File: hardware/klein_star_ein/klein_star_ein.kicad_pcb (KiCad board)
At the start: 6 copper layers, 171 parts, among them J1 USB_A, J2 DB15_Female_HighDensity_Mount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, U1 ECP5UM25, U2 MT41K512M16, U3 MT41K512M16, U4 FT2232HQ, U5 W25Q128JVS, U6 USB3300-EZK, U7 USB3300-EZK

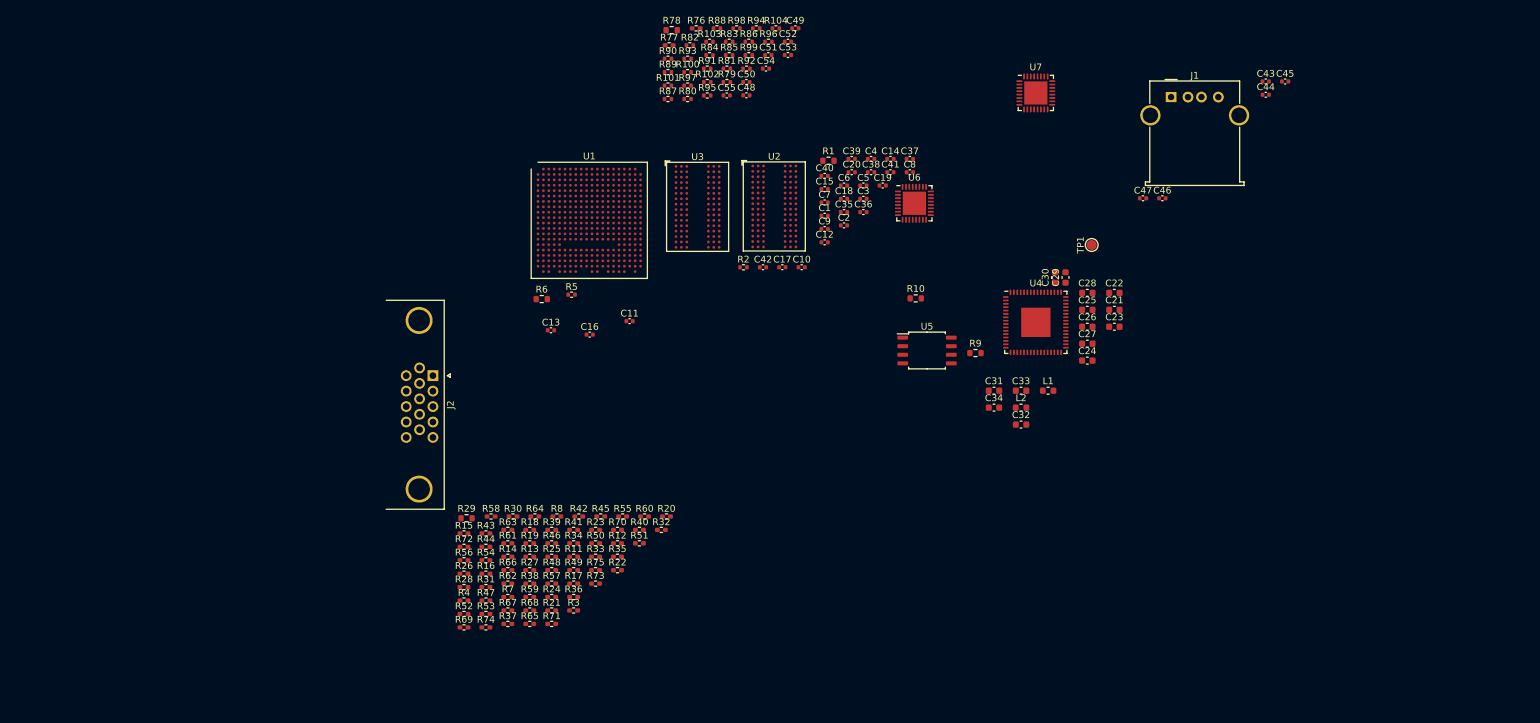
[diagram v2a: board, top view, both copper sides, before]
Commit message: VGA phy schematic and layout
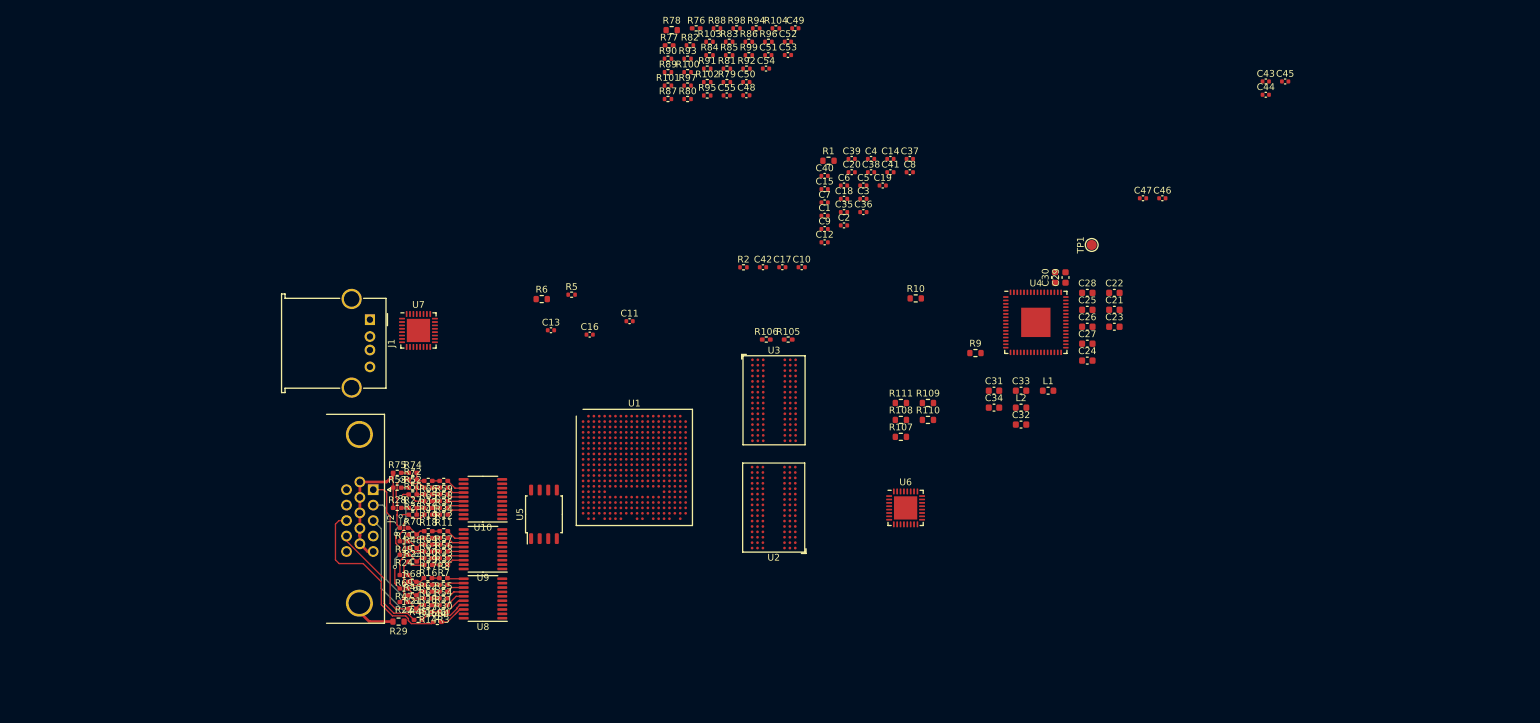
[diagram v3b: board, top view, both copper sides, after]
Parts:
- removed R13, R20, R26, R36, R43, R51, R60, R67, R73: R, Resistor_SMD:R_0402_1005Metric_Pad0.72x0.64mm_HandSolder
- added R105: 0R, Resistor_SMD:R_0402_1005Metric_Pad0.72x0.64mm_HandSolder, F.Cu at (167.2, 106.4)
- added R106: 0R, Resistor_SMD:R_0402_1005Metric_Pad0.72x0.64mm_HandSolder, F.Cu at (163.9, 106.4)
- added R107: 10k, Resistor_SMD:R_0603_1608Metric, F.Cu at (183.8, 120.8)
- added R108: 0R, Resistor_SMD:R_0603_1608Metric, F.Cu at (183.8, 118.3)
- added R109: 0R, Resistor_SMD:R_0603_1608Metric, F.Cu at (187.9, 115.8)
- added R110: 0R, Resistor_SMD:R_0603_1608Metric, F.Cu at (187.9, 118.3)
- added R111: 0R, Resistor_SMD:R_0603_1608Metric, F.Cu at (183.8, 115.8)
- added U10: SN74ALVC245PWR, Package_SO:TSSOP-20_4.4x6.5mm_P0.65mm, F.Cu at (121.9, 130.1)
- added U8: SN74ALVC245PWR, Package_SO:TSSOP-20_4.4x6.5mm_P0.65mm, F.Cu at (121.9, 144.8)
- added U9: SN74ALVC245PWR, Package_SO:TSSOP-20_4.4x6.5mm_P0.65mm, F.Cu at (121.9, 137.5)
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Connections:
- net Net-(U6-Pad14) renamed /USB_SLAVE_CLKOUT
- net Net-(U6-Pad28) renamed /USB_SLAVE_CLK
- net Net-(U6-Pad9) renamed /USB_SLAVE_RESET
- J1 pad 1: Net-(J1-Pad1) -> unconnected-(J1-Pad1)
- J2 pad 11: no_connect_462 -> unconnected-(J2-Pad11)
- J2 pad 12: no_connect_463 -> unconnected-(J2-Pad12)
- J2 pad 15: no_connect_464 -> unconnected-(J2-Pad15)
- J2 pad 4: no_connect_465 -> unconnected-(J2-Pad4)
- R27 pad 2: Net-(R20-Pad2) -> Net-(R19-Pad2)
- R52 pad 2: Net-(R43-Pad2) -> Net-(R42-Pad2)
- R74 pad 2: Net-(R67-Pad2) -> Net-(R66-Pad2)
- U1 pad A12: Net-(U1-PadA12) -> unconnected-(U1-PadA12)
- U1 pad A13: Net-(U1-PadA13) -> unconnected-(U1-PadA13)
- U1 pad A14: Net-(U1-PadA14) -> unconnected-(U1-PadA14)
- U1 pad A15: no_connect_466 -> unconnected-(U1-PadA15)
- U1 pad A16: Net-(U1-PadA16) -> unconnected-(U1-PadA16)
- U1 pad A17: Net-(U1-PadA17) -> unconnected-(U1-PadA17)
- U1 pad A18: Net-(U1-PadA18) -> unconnected-(U1-PadA18)
- U1 pad A19: Net-(U1-PadA19) -> unconnected-(U1-PadA19)
- U1 pad A2: Net-(U1-PadA2) -> unconnected-(U1-PadA2)
- U1 pad A3: Net-(U1-PadA3) -> unconnected-(U1-PadA3)
- U1 pad A4: Net-(U1-PadA4) -> unconnected-(U1-PadA4)
- U1 pad A5: Net-(U1-PadA5) -> unconnected-(U1-PadA5)
- U1 pad B1: Net-(U1-PadB1) -> unconnected-(U1-PadB1)
- U1 pad B12: Net-(U1-PadB12) -> unconnected-(U1-PadB12)
- U1 pad B13: Net-(U1-PadB13) -> unconnected-(U1-PadB13)
- U1 pad B15: Net-(U1-PadB15) -> unconnected-(U1-PadB15)
- U1 pad B16: Net-(U1-PadB16) -> unconnected-(U1-PadB16)
- U1 pad B17: Net-(U1-PadB17) -> unconnected-(U1-PadB17)
- U1 pad B18: Net-(U1-PadB18) -> unconnected-(U1-PadB18)
- U1 pad B19: Net-(U1-PadB19) -> unconnected-(U1-PadB19)
- U1 pad B2: Net-(U1-PadB2) -> unconnected-(U1-PadB2)
- U1 pad B20: Net-(U1-PadB20) -> unconnected-(U1-PadB20)
- U1 pad B3: Net-(U1-PadB3) -> unconnected-(U1-PadB3)
- U1 pad B4: Net-(U1-PadB4) -> unconnected-(U1-PadB4)
- U1 pad B5: Net-(U1-PadB5) -> unconnected-(U1-PadB5)
- U1 pad C1: Net-(U1-PadC1) -> unconnected-(U1-PadC1)
- U1 pad C12: Net-(U1-PadC12) -> unconnected-(U1-PadC12)
- U1 pad C13: Net-(U1-PadC13) -> unconnected-(U1-PadC13)
- U1 pad C14: Net-(U1-PadC14) -> unconnected-(U1-PadC14)
- U1 pad C15: Net-(U1-PadC15) -> unconnected-(U1-PadC15)
- U1 pad C16: Net-(U1-PadC16) -> unconnected-(U1-PadC16)
- U1 pad C17: Net-(U1-PadC17) -> unconnected-(U1-PadC17)
- U1 pad C18: Net-(U1-PadC18) -> unconnected-(U1-PadC18)
- U1 pad C2: Net-(U1-PadC2) -> unconnected-(U1-PadC2)
- U1 pad C20: Net-(U1-PadC20) -> unconnected-(U1-PadC20)
- U1 pad C3: Net-(U1-PadC3) -> unconnected-(U1-PadC3)
- U1 pad C4: Net-(U1-PadC4) -> unconnected-(U1-PadC4)
- U1 pad C5: Net-(U1-PadC5) -> unconnected-(U1-PadC5)
- U1 pad C9: no_connect_467 -> unconnected-(U1-PadC9)
- U1 pad D1: Net-(U1-PadD1) -> unconnected-(U1-PadD1)
- U1 pad D10: no_connect_468 -> unconnected-(U1-PadD10)
- U1 pad D11: Net-(U1-PadD11) -> unconnected-(U1-PadD11)
- U1 pad D12: Net-(U1-PadD12) -> unconnected-(U1-PadD12)
- U1 pad D13: Net-(U1-PadD13) -> unconnected-(U1-PadD13)
- U1 pad D14: Net-(U1-PadD14) -> unconnected-(U1-PadD14)
- U1 pad D15: Net-(U1-PadD15) -> unconnected-(U1-PadD15)
- U1 pad D16: Net-(U1-PadD16) -> unconnected-(U1-PadD16)
- U1 pad D17: Net-(U1-PadD17) -> unconnected-(U1-PadD17)
- U1 pad D18: Net-(U1-PadD18) -> unconnected-(U1-PadD18)
- U1 pad D19: Net-(U1-PadD19) -> unconnected-(U1-PadD19)
- U1 pad D2: Net-(U1-PadD2) -> unconnected-(U1-PadD2)
- U1 pad D20: Net-(U1-PadD20) -> unconnected-(U1-PadD20)
- U1 pad D3: Net-(U1-PadD3) -> unconnected-(U1-PadD3)
- U1 pad D5: Net-(U1-PadD5) -> unconnected-(U1-PadD5)
- U1 pad E1: Net-(U1-PadE1) -> unconnected-(U1-PadE1)
- U1 pad E10: no_connect_469 -> unconnected-(U1-PadE10)
- U1 pad E11: Net-(U1-PadE11) -> unconnected-(U1-PadE11)
- U1 pad E12: Net-(U1-PadE12) -> unconnected-(U1-PadE12)
- U1 pad E13: Net-(U1-PadE13) -> unconnected-(U1-PadE13)
- U1 pad E14: Net-(U1-PadE14) -> unconnected-(U1-PadE14)
- U1 pad E15: Net-(U1-PadE15) -> unconnected-(U1-PadE15)
- U1 pad E16: Net-(U1-PadE16) -> unconnected-(U1-PadE16)
- U1 pad E17: Net-(U1-PadE17) -> unconnected-(U1-PadE17)
- U1 pad E18: Net-(U1-PadE18) -> unconnected-(U1-PadE18)
- U1 pad E19: Net-(U1-PadE19) -> unconnected-(U1-PadE19)
- U1 pad E2: Net-(U1-PadE2) -> unconnected-(U1-PadE2)
- U1 pad E20: Net-(U1-PadE20) -> unconnected-(U1-PadE20)
- U1 pad E3: Net-(U1-PadE3) -> unconnected-(U1-PadE3)
- U1 pad E4: Net-(U1-PadE4) -> unconnected-(U1-PadE4)
- U1 pad E5: Net-(U1-PadE5) -> unconnected-(U1-PadE5)
- U1 pad F1: Net-(U1-PadF1) -> unconnected-(U1-PadF1)
- U1 pad F10: Net-(U1-PadF10) -> unconnected-(U1-PadF10)
- U1 pad F11: Net-(U1-PadF11) -> unconnected-(U1-PadF11)
- U1 pad F12: Net-(U1-PadF12) -> unconnected-(U1-PadF12)
- U1 pad F15: Net-(U1-PadF15) -> unconnected-(U1-PadF15)
- U1 pad F16: Net-(U1-PadF16) -> unconnected-(U1-PadF16)
- U1 pad F17: Net-(U1-PadF17) -> unconnected-(U1-PadF17)
- U1 pad F18: Net-(U1-PadF18) -> unconnected-(U1-PadF18)
- U1 pad F19: Net-(U1-PadF19) -> unconnected-(U1-PadF19)
- U1 pad F2: Net-(U1-PadF2) -> unconnected-(U1-PadF2)
- U1 pad F20: Net-(U1-PadF20) -> unconnected-(U1-PadF20)
- U1 pad F3: Net-(U1-PadF3) -> unconnected-(U1-PadF3)
- U1 pad F4: Net-(U1-PadF4) -> unconnected-(U1-PadF4)
- U1 pad F5: Net-(U1-PadF5) -> unconnected-(U1-PadF5)
- U1 pad F6: Net-(U1-PadF6) -> unconnected-(U1-PadF6)
- U1 pad F9: Net-(U1-PadF9) -> unconnected-(U1-PadF9)
- U1 pad G1: Net-(U1-PadG1) -> unconnected-(U1-PadG1)
- U1 pad G16: Net-(U1-PadG16) -> unconnected-(U1-PadG16)
- U1 pad G18: Net-(U1-PadG18) -> unconnected-(U1-PadG18)
- U1 pad G19: Net-(U1-PadG19) -> unconnected-(U1-PadG19)
- U1 pad G2: Net-(U1-PadG2) -> unconnected-(U1-PadG2)
- U1 pad G20: Net-(U1-PadG20) -> unconnected-(U1-PadG20)
- U1 pad G3: Net-(U1-PadG3) -> unconnected-(U1-PadG3)
- U1 pad G5: Net-(U1-PadG5) -> unconnected-(U1-PadG5)
- U1 pad H1: Net-(U1-PadH1) -> unconnected-(U1-PadH1)
- U1 pad H10: Net-(U1-PadH10) -> unconnected-(U1-PadH10)
- U1 pad H11: Net-(U1-PadH11) -> unconnected-(U1-PadH11)
- U1 pad H12: Net-(U1-PadH12) -> unconnected-(U1-PadH12)
- U1 pad H13: Net-(U1-PadH13) -> unconnected-(U1-PadH13)
- U1 pad H14: Net-(U1-PadH14) -> unconnected-(U1-PadH14)
- U1 pad H15: Net-(U1-PadH15) -> unconnected-(U1-PadH15)
- U1 pad H16: Net-(U1-PadH16) -> unconnected-(U1-PadH16)
- U1 pad H17: Net-(U1-PadH17) -> unconnected-(U1-PadH17)
- U1 pad H18: Net-(U1-PadH18) -> unconnected-(U1-PadH18)
- U1 pad H2: Net-(U1-PadH2) -> unconnected-(U1-PadH2)
- U1 pad H20: Net-(U1-PadH20) -> unconnected-(U1-PadH20)
- U1 pad H3: Net-(U1-PadH3) -> unconnected-(U1-PadH3)
- U1 pad H4: Net-(U1-PadH4) -> unconnected-(U1-PadH4)
- U1 pad H5: Net-(U1-PadH5) -> unconnected-(U1-PadH5)
- U1 pad H6: Net-(U1-PadH6) -> unconnected-(U1-PadH6)
- U1 pad H7: Net-(U1-PadH7) -> unconnected-(U1-PadH7)
- U1 pad H8: Net-(U1-PadH8) -> unconnected-(U1-PadH8)
- U1 pad H9: Net-(U1-PadH9) -> unconnected-(U1-PadH9)
- U1 pad J1: Net-(U1-PadJ1) -> unconnected-(U1-PadJ1)
- U1 pad J13: Net-(U1-PadJ13) -> unconnected-(U1-PadJ13)
- U1 pad J15: Net-(U1-PadJ15) -> unconnected-(U1-PadJ15)
- U1 pad J16: Net-(U1-PadJ16) -> unconnected-(U1-PadJ16)
- U1 pad J17: Net-(U1-PadJ17) -> unconnected-(U1-PadJ17)
- U1 pad J18: Net-(U1-PadJ18) -> unconnected-(U1-PadJ18)
- U1 pad J19: Net-(U1-PadJ19) -> unconnected-(U1-PadJ19)
- U1 pad J20: Net-(U1-PadJ20) -> unconnected-(U1-PadJ20)
- U1 pad J3: Net-(U1-PadJ3) -> unconnected-(U1-PadJ3)
- U1 pad J4: Net-(U1-PadJ4) -> unconnected-(U1-PadJ4)
- U1 pad J5: Net-(U1-PadJ5) -> unconnected-(U1-PadJ5)
- U1 pad J6: Net-(U1-PadJ6) -> unconnected-(U1-PadJ6)
- U1 pad J8: Net-(U1-PadJ8) -> unconnected-(U1-PadJ8)
- U1 pad K1: Net-(U1-PadK1) -> unconnected-(U1-PadK1)
- U1 pad K13: Net-(U1-PadK13) -> unconnected-(U1-PadK13)
- U1 pad K16: no_connect_470 -> unconnected-(U1-PadK16)
- U1 pad K17: no_connect_471 -> unconnected-(U1-PadK17)
- U1 pad K18: Net-(U1-PadK18) -> unconnected-(U1-PadK18)
- U1 pad K19: Net-(U1-PadK19) -> unconnected-(U1-PadK19)
- U1 pad K2: Net-(U1-PadK2) -> unconnected-(U1-PadK2)
- U1 pad K20: Net-(U1-PadK20) -> unconnected-(U1-PadK20)
- U1 pad K3: Net-(U1-PadK3) -> unconnected-(U1-PadK3)
- U1 pad K4: Net-(U1-PadK4) -> unconnected-(U1-PadK4)
- U1 pad K5: Net-(U1-PadK5) -> unconnected-(U1-PadK5)
- U1 pad K8: Net-(U1-PadK8) -> unconnected-(U1-PadK8)
- U1 pad L1: Net-(U1-PadL1) -> unconnected-(U1-PadL1)
- U1 pad L13: Net-(U1-PadL13) -> unconnected-(U1-PadL13)
- U1 pad L14: Net-(U1-PadL14) -> unconnected-(U1-PadL14)
- U1 pad L15: Net-(U1-PadL15) -> unconnected-(U1-PadL15)
- U1 pad L16: Net-(U1-PadL16) -> unconnected-(U1-PadL16)
- U1 pad L17: Net-(U1-PadL17) -> unconnected-(U1-PadL17)
- U1 pad L18: Net-(U1-PadL18) -> unconnected-(U1-PadL18)
- U1 pad L19: Net-(U1-PadL19) -> unconnected-(U1-PadL19)
- U1 pad L2: Net-(U1-PadL2) -> unconnected-(U1-PadL2)
- U1 pad L20: Net-(U1-PadL20) -> unconnected-(U1-PadL20)
- U1 pad L3: Net-(U1-PadL3) -> unconnected-(U1-PadL3)
- U1 pad L4: Net-(U1-PadL4) -> unconnected-(U1-PadL4)
- U1 pad L5: Net-(U1-PadL5) -> unconnected-(U1-PadL5)
- U1 pad L6: Net-(U1-PadL6) -> unconnected-(U1-PadL6)
- U1 pad L7: Net-(U1-PadL7) -> unconnected-(U1-PadL7)
- U1 pad L8: Net-(U1-PadL8) -> unconnected-(U1-PadL8)
- U1 pad M1: Net-(U1-PadM1) -> unconnected-(U1-PadM1)
- U1 pad M13: Net-(U1-PadM13) -> unconnected-(U1-PadM13)
- U1 pad M15: Net-(U1-PadM15) -> unconnected-(U1-PadM15)
- U1 pad M17: Net-(U1-PadM17) -> unconnected-(U1-PadM17)
- U1 pad M18: Net-(U1-PadM18) -> unconnected-(U1-PadM18)
- U1 pad M19: Net-(U1-PadM19) -> unconnected-(U1-PadM19)
- U1 pad M20: Net-(U1-PadM20) -> unconnected-(U1-PadM20)
- U1 pad M3: Net-(U1-PadM3) -> unconnected-(U1-PadM3)
- U1 pad M4: Net-(U1-PadM4) -> unconnected-(U1-PadM4)
- U1 pad M5: no_connect_472 -> unconnected-(U1-PadM5)
- U1 pad M6: Net-(U1-PadM6) -> unconnected-(U1-PadM6)
- U1 pad M8: Net-(U1-PadM8) -> unconnected-(U1-PadM8)
- U1 pad N1: Net-(U1-PadN1) -> unconnected-(U1-PadN1)
- U1 pad N10: Net-(U1-PadN10) -> unconnected-(U1-PadN10)
- U1 pad N11: Net-(U1-PadN11) -> unconnected-(U1-PadN11)
- U1 pad N12: Net-(U1-PadN12) -> unconnected-(U1-PadN12)
- U1 pad N13: Net-(U1-PadN13) -> unconnected-(U1-PadN13)
- U1 pad N16: Net-(U1-PadN16) -> unconnected-(U1-PadN16)
- U1 pad N17: Net-(U1-PadN17) -> unconnected-(U1-PadN17)
- U1 pad N18: Net-(U1-PadN18) -> unconnected-(U1-PadN18)
- U1 pad N19: Net-(U1-PadN19) -> unconnected-(U1-PadN19)
- U1 pad N2: Net-(U1-PadN2) -> unconnected-(U1-PadN2)
- U1 pad N20: Net-(U1-PadN20) -> unconnected-(U1-PadN20)
- U1 pad N3: Net-(U1-PadN3) -> unconnected-(U1-PadN3)
- U1 pad N4: Net-(U1-PadN4) -> unconnected-(U1-PadN4)
- U1 pad N5: Net-(U1-PadN5) -> unconnected-(U1-PadN5)
- U1 pad N8: Net-(U1-PadN8) -> unconnected-(U1-PadN8)
- U1 pad N9: Net-(U1-PadN9) -> unconnected-(U1-PadN9)
- U1 pad P1: Net-(U1-PadP1) -> unconnected-(U1-PadP1)
- U1 pad P15: Net-(U1-PadP15) -> unconnected-(U1-PadP15)
- U1 pad P16: Net-(U1-PadP16) -> unconnected-(U1-PadP16)
- U1 pad P17: Net-(U1-PadP17) -> unconnected-(U1-PadP17)
- U1 pad P18: Net-(U1-PadP18) -> unconnected-(U1-PadP18)
- U1 pad P19: Net-(U1-PadP19) -> unconnected-(U1-PadP19)
- U1 pad P2: Net-(U1-PadP2) -> unconnected-(U1-PadP2)
- U1 pad P20: Net-(U1-PadP20) -> unconnected-(U1-PadP20)
- U1 pad P3: Net-(U1-PadP3) -> unconnected-(U1-PadP3)
- U1 pad P4: Net-(U1-PadP4) -> unconnected-(U1-PadP4)
- U1 pad P5: Net-(U1-PadP5) -> unconnected-(U1-PadP5)
- U1 pad P6: Net-(U1-PadP6) -> unconnected-(U1-PadP6)
- U1 pad R16: Net-(U1-PadR16) -> unconnected-(U1-PadR16)
- U1 pad R17: Net-(U1-PadR17) -> unconnected-(U1-PadR17)
- U1 pad R18: Net-(U1-PadR18) -> unconnected-(U1-PadR18)
- U1 pad R20: Net-(U1-PadR20) -> unconnected-(U1-PadR20)
- U1 pad R5: Net-(U1-PadR5) -> unconnected-(U1-PadR5)
- U1 pad T10: Net-(U1-PadT10) -> unconnected-(U1-PadT10)
- U1 pad T11: no_connect_473 -> unconnected-(U1-PadT11)
- U1 pad T12: no_connect_474 -> unconnected-(U1-PadT12)
- U1 pad T13: no_connect_475 -> unconnected-(U1-PadT13)
- U1 pad T14: no_connect_476 -> unconnected-(U1-PadT14)
- U1 pad T15: no_connect_477 -> unconnected-(U1-PadT15)
- U1 pad T16: no_connect_478 -> unconnected-(U1-PadT16)
- U1 pad T17: Net-(U1-PadT17) -> unconnected-(U1-PadT17)
- U1 pad T18: Net-(U1-PadT18) -> unconnected-(U1-PadT18)
- U1 pad T19: Net-(U1-PadT19) -> unconnected-(U1-PadT19)
- U1 pad T20: Net-(U1-PadT20) -> unconnected-(U1-PadT20)
- U1 pad T5: Net-(U1-PadT5) -> unconnected-(U1-PadT5)
- U1 pad T6: Net-(U1-PadT6) -> unconnected-(U1-PadT6)
- U1 pad T7: Net-(U1-PadT7) -> unconnected-(U1-PadT7)
- U1 pad T8: Net-(U1-PadT8) -> unconnected-(U1-PadT8)
- U1 pad T9: Net-(U1-PadT9) -> unconnected-(U1-PadT9)
- U1 pad U15: no_connect_479 -> unconnected-(U1-PadU15)
- U1 pad U16: Net-(U1-PadU16) -> unconnected-(U1-PadU16)
- U1 pad U17: Net-(U1-PadU17) -> unconnected-(U1-PadU17)
- U1 pad U18: Net-(U1-PadU18) -> unconnected-(U1-PadU18)
- U1 pad U19: Net-(U1-PadU19) -> unconnected-(U1-PadU19)
- U1 pad U20: Net-(U1-PadU20) -> unconnected-(U1-PadU20)
- U1 pad U5: Net-(U1-PadU5) -> unconnected-(U1-PadU5)
- U1 pad U6: Net-(U1-PadU6) -> unconnected-(U1-PadU6)
- U1 pad V10: Net-(U1-PadV10) -> unconnected-(U1-PadV10)
- U1 pad V11: Net-(U1-PadV11) -> unconnected-(U1-PadV11)
- U1 pad V17: no_connect_480 -> unconnected-(U1-PadV17)
- U1 pad V18: no_connect_481 -> unconnected-(U1-PadV18)
- U1 pad V4: Net-(U1-PadV4) -> unconnected-(U1-PadV4)
- U1 pad W10: Net-(U1-PadW10) -> unconnected-(U1-PadW10)
- U1 pad W11: Net-(U1-PadW11) -> unconnected-(U1-PadW11)
- U1 pad W13: no_connect_482 -> unconnected-(U1-PadW13)
- U1 pad W14: no_connect_483 -> unconnected-(U1-PadW14)
- U1 pad W17: no_connect_484 -> unconnected-(U1-PadW17)
- U1 pad W18: no_connect_485 -> unconnected-(U1-PadW18)
- U1 pad W20: no_connect_486 -> unconnected-(U1-PadW20)
- U1 pad W4: Net-(U1-PadW4) -> unconnected-(U1-PadW4)
- U1 pad W5: Net-(U1-PadW5) -> unconnected-(U1-PadW5)
- U1 pad W8: Net-(U1-PadW8) -> unconnected-(U1-PadW8)
- U1 pad W9: Net-(U1-PadW9) -> unconnected-(U1-PadW9)
- U1 pad Y11: Net-(U1-PadY11) -> unconnected-(U1-PadY11)
- U1 pad Y12: Net-(U1-PadY12) -> unconnected-(U1-PadY12)
- U1 pad Y14: no_connect_487 -> unconnected-(U1-PadY14)
- U1 pad Y15: no_connect_488 -> unconnected-(U1-PadY15)
- U1 pad Y16: no_connect_489 -> unconnected-(U1-PadY16)
- U1 pad Y17: no_connect_490 -> unconnected-(U1-PadY17)
- U1 pad Y19: no_connect_491 -> unconnected-(U1-PadY19)
- U1 pad Y5: Net-(U1-PadY5) -> unconnected-(U1-PadY5)
- U1 pad Y6: Net-(U1-PadY6) -> unconnected-(U1-PadY6)
- U1 pad Y7: Net-(U1-PadY7) -> unconnected-(U1-PadY7)
- U1 pad Y8: Net-(U1-PadY8) -> unconnected-(U1-PadY8)
- U2 pad J1: no_connect_492 -> unconnected-(U2-PadJ1)
- U2 pad J9: no_connect_493 -> unconnected-(U2-PadJ9)
- U2 pad L1: no_connect_494 -> unconnected-(U2-PadL1)
- U2 pad L9: no_connect_495 -> unconnected-(U2-PadL9)
- U3 pad J1: no_connect_496 -> unconnected-(U3-PadJ1)
- U3 pad J9: no_connect_497 -> unconnected-(U3-PadJ9)
- U3 pad L1: no_connect_498 -> unconnected-(U3-PadL1)
- U3 pad L9: no_connect_499 -> unconnected-(U3-PadL9)
- U4 pad 16: /JTAG_TCK -> Net-(U4-Pad16)
- U4 pad 17: /JTAG_TDI -> Net-(U4-Pad17)
- U4 pad 18: /JTAG_TDO -> Net-(U4-Pad18)
- U4 pad 19: /JTAG_TMS -> Net-(U4-Pad19)
- U4 pad 2: Net-(U4-Pad2) -> unconnected-(U4-Pad2)
- U4 pad 21: no_connect_500 -> unconnected-(U4-Pad21)
- U4 pad 22: no_connect_501 -> unconnected-(U4-Pad22)
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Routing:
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
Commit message: power failure
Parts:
- removed R100, R101, R102, R103, R104, R81, R82, R83, R84, R85, R86, R87, R88, R89, R90, R91, R92, R93, R94, R95, R96, R97, R98, R99: 51R, Resistor_SMD:R_0402_1005Metric
- added C56: 100nF, Capacitor_SMD:C_0402_1005Metric, F.Cu at (118.7, 116.5)
- added C57: 100nF, Capacitor_SMD:C_0402_1005Metric, F.Cu at (115.1, 115.5)
- added C58: 470n, Capacitor_SMD:C_0402_1005Metric, F.Cu at (182.0, 134.5)
- added C59: 100nF, Capacitor_SMD:C_0402_1005Metric, F.Cu at (118.4, 125.1)
- added C60: 100nF, Capacitor_SMD:C_0402_1005Metric, F.Cu at (78.6, 118.2)
- added C61: 4u7, Capacitor_SMD:C_0603_1608Metric, F.Cu at (78.4, 102.0)
- added C62: 4u7, Capacitor_SMD:C_0603_1608Metric, F.Cu at (75.0, 105.5)
- added C63: 4u7, Capacitor_SMD:C_0402_1005Metric, F.Cu at (117.9, 148.8)
- added C64: 4u7, Capacitor_SMD:C_0402_1005Metric, F.Cu at (116.9, 140.8)
- added C65: 4u7, Capacitor_SMD:C_0402_1005Metric, F.Cu at (116.4, 133.6)
- added J10: AudioJack3_Ground_Switch, Connector_Audio:Jack_3.5mm_CUI_SJ1-3535NG_Horizontal, F.Cu at (196.8, 96.4)
- added J11: AudioJack3_Ground_Switch, Connector_Audio:Jack_3.5mm_CUI_SJ1-3535NG_Horizontal, F.Cu at (196.8, 115.4)
- added J12: AudioJack3_Ground_Switch, Connector_Audio:Jack_3.5mm_CUI_SJ1-3535NG_Horizontal, F.Cu at (99.3, 83.0)
- added J3: Bus_PCI_Express_x1, Connector_PCBEdge:BUS_PCIexpress_x1, F.Cu at (143.6, 154.9)
- added J4: 1367073-1, Connector:Connector_SFP_and_Cage, F.Cu at (140.0, 69.0)
- added J5: RJ45_LED_Shielded, Connector_RJ:RJ45_Amphenol_RJHSE538X, F.Cu at (102.9, 110.2)
- added J6: USB_C_Receptacle, Connector_USB:USB_C_Receptacle_GCT_USB4085, F.Cu at (195.0, 67.0)
- added J7: MEM2051-00-195-00-A, footprints:MEM2051-00-195-00-A, F.Cu at (190.5, 84.0)
- added J8: AudioJack3_Ground_Switch, Connector_Audio:Jack_3.5mm_CUI_SJ1-3535NG_Horizontal, F.Cu at (196.8, 124.9)
- added J9: AudioJack3_Ground_Switch, Connector_Audio:Jack_3.5mm_CUI_SJ1-3535NG_Horizontal, F.Cu at (196.8, 105.9)
- added R13: 12k 1%, Resistor_SMD:R_0603_1608Metric, F.Cu at (112.6, 117.2)
- added R20: 10k, Resistor_SMD:R_0402_1005Metric_Pad0.72x0.64mm_HandSolder, F.Cu at (80.0, 105.2)
- added R26: 1k, Resistor_SMD:R_0402_1005Metric_Pad0.72x0.64mm_HandSolder, F.Cu at (73.4, 113.5)
- added R36: 1k, Resistor_SMD:R_0402_1005Metric_Pad0.72x0.64mm_HandSolder, F.Cu at (112.1, 121.0)
- added RN1: 51R, Resistor_SMD:R_Array_Concave_4x0402, F.Cu at (172.0, 127.2)
- added RN2: 51R, Resistor_SMD:R_Array_Concave_4x0402, F.Cu at (172.0, 129.7)
- added RN3: 51R, Resistor_SMD:R_Array_Concave_4x0402, F.Cu at (177.9, 129.1)
- added RN4: 51R, Resistor_SMD:R_Array_Concave_4x0402, F.Cu at (172.0, 132.4)
- added RN5: 51R, Resistor_SMD:R_Array_Concave_4x0402, F.Cu at (172.0, 134.9)
- added RN6: 51R, Resistor_SMD:R_Array_Concave_4x0402, F.Cu at (172.0, 123.8)
- added RN7: 51R, Resistor_SMD:R_Array_Concave_4x0402, F.Cu at (172.0, 121.2)
- added RN8: 51R, Resistor_SMD:R_Array_Concave_4x0402, F.Cu at (172.0, 118.6)
- added TP2: 1V8, TestPoint:TestPoint_Pad_D1.0mm, F.Cu at (77.0, 119.0)
- added U11: KSZ9021RL, Package_QFP:LQFP-64-1EP_10x10mm_P0.5mm_EP6.5x6.5mm, F.Cu at (130.0, 87.5)
- added U12: TUSB2036, Package_QFP:LQFP-32_7x7mm_P0.8mm, F.Cu at (149.9, 99.6)
- added U13: TPS2041B, Package_TO_SOT_SMD:SOT-23-5, F.Cu at (77.6, 105.2)
- C27, C31, C32, C33, C34, C40, L1, L2: moved to B.Cu
- J1: footprint Connector_USB:USB_A_Molex_67643_Horizontal -> Connector_USB:USB_A_Wuerth_614004134726_Horizontal
- moved TP1 147.7 mm to (64.7, 102.0), turned to 180 degrees
- moved C45 132.4 mm to (120.6, 123.7)
- moved C43 132.4 mm to (115.1, 117.5), turned to 180 degrees
- moved C44 128.4 mm to (118.7, 117.5)
- moved C46 116.4 mm to (112.2, 122.1), turned to 180 degrees
- moved C47 109.2 mm to (115.1, 116.5), turned to 180 degrees
- moved C49 105.0 mm to (75.5, 109.6), turned to 90 degrees
- moved C51 103.7 mm to (73.6, 114.8), turned to 180 degrees
- moved R107 101.2 mm to (83.0, 112.2), turned to -135 degrees
- moved C52 99.1 mm to (80.0, 109.6), turned to 90 degrees
- moved C53 99.1 mm to (79.0, 109.6), turned to 90 degrees
- moved C54 96.6 mm to (77.5, 109.6), turned to -90 degrees
- moved C50 94.8 mm to (80.1, 117.7)
- moved R76 94.6 mm to (74.1, 111.7), turned to 90 degrees
- moved C48 93.2 mm to (76.5, 109.6), turned to 90 degrees
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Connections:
- net Net-(C1-Pad1) renamed /DRAM_1_VCORE
- net Net-(C10-Pad1) renamed /DRAM_2_VCORE
- J1 pad 1: unconnected-(J1-Pad1) -> /USB_SLAVE_vBUS
- R44 pad 2: /VGA_HSYNC -> /VGA_BUF_HSYNC
- R45 pad 2: /VGA_VSYNC -> /VGA_BUF_VSYNC
- U1 pad A2: unconnected-(U1-PadA2) -> /FIFO_D1/TX
- U1 pad A3: unconnected-(U1-PadA3) -> /FIFO_D3
- U1 pad A4: unconnected-(U1-PadA4) -> /FIFO_D5
- U1 pad A5: unconnected-(U1-PadA5) -> /FIFO_D7
- U1 pad B1: unconnected-(U1-PadB1) -> /USB_SLAVE_DATA0
- U1 pad B2: unconnected-(U1-PadB2) -> /USB_SLAVE_DATA1
- U1 pad B3: unconnected-(U1-PadB3) -> /FIFO_D0/RX
- U1 pad B4: unconnected-(U1-PadB4) -> /FIFO_D2
- U1 pad B5: unconnected-(U1-PadB5) -> /FIFO_D4
- U1 pad C1: unconnected-(U1-PadC1) -> /USB_SLAVE_DATA2
- U1 pad C18: unconnected-(U1-PadC18) -> /DRAM_nWE
- U1 pad C2: unconnected-(U1-PadC2) -> /USB_SLAVE_DATA3
- U1 pad C20: unconnected-(U1-PadC20) -> /DRAM_nCS
- U1 pad C3: unconnected-(U1-PadC3) -> /FIFO_nTXE
- U1 pad C4: unconnected-(U1-PadC4) -> /FIFO_nRXE
- U1 pad C5: unconnected-(U1-PadC5) -> /FIFO_D6
- U1 pad D1: unconnected-(U1-PadD1) -> /USB_SLAVE_DATA4
- U1 pad D17: unconnected-(U1-PadD17) -> /DRAM_ADDR_BA0
- U1 pad D18: unconnected-(U1-PadD18) -> /DRAM_ADDR_BA2
- U1 pad D2: unconnected-(U1-PadD2) -> /USB_SLAVE_DATA5
- U1 pad D3: unconnected-(U1-PadD3) -> /FIFO_nWR
- U1 pad D5: unconnected-(U1-PadD5) -> /FIFO_nRD
- U1 pad E1: unconnected-(U1-PadE1) -> /USB_SLAVE_DATA6
- U1 pad E16: unconnected-(U1-PadE16) -> /DRAM_ADDR_3
- U1 pad E17: unconnected-(U1-PadE17) -> /DRAM_ADDR_0
- U1 pad E2: unconnected-(U1-PadE2) -> /USB_SLAVE_DATA7
- U1 pad E3: unconnected-(U1-PadE3) -> /USB_SLAVE_RESET
- U1 pad E4: unconnected-(U1-PadE4) -> /USB_SLAVE_CLK
- U1 pad E5: unconnected-(U1-PadE5) -> /FIFO_WKUP
- U1 pad F1: unconnected-(U1-PadF1) -> /VGA_B_5
- U1 pad F3: unconnected-(U1-PadF3) -> /USB_SLAVE_NXT
- U1 pad F4: unconnected-(U1-PadF4) -> /USB_SLAVE_DIR
- U1 pad F5: unconnected-(U1-PadF5) -> /USB_SLAVE_CLKOUT
- U1 pad G1: unconnected-(U1-PadG1) -> /VGA_G_5
- U1 pad G2: unconnected-(U1-PadG2) -> /VGA_G_4
- U1 pad G3: unconnected-(U1-PadG3) -> /USB_SLAVE_STP
- U1 pad H1: unconnected-(U1-PadH1) -> /VGA_R_5
- U1 pad H10: unconnected-(U1-PadH10) -> /FPGA_VCORE
- U1 pad H11: unconnected-(U1-PadH11) -> /FPGA_VCORE
- U1 pad H12: unconnected-(U1-PadH12) -> /FPGA_VCORE
- U1 pad H13: unconnected-(U1-PadH13) -> /FPGA_VCORE
- U1 pad H14: unconnected-(U1-PadH14) -> +1V35
- U1 pad H15: unconnected-(U1-PadH15) -> +1V35
- U1 pad H2: unconnected-(U1-PadH2) -> /VGA_R_4
- U1 pad H6: unconnected-(U1-PadH6) -> Net-(U1-PadH6)
- U1 pad H7: unconnected-(U1-PadH7) -> Net-(U1-PadH6)
- U1 pad H8: unconnected-(U1-PadH8) -> /FPGA_VCORE
- U1 pad H9: unconnected-(U1-PadH9) -> /FPGA_VCORE
- U1 pad J1: unconnected-(U1-PadJ1) -> /VGA_B_3
- U1 pad J13: unconnected-(U1-PadJ13) -> /FPGA_VCORE
- U1 pad J15: unconnected-(U1-PadJ15) -> +1V35
- U1 pad J16: unconnected-(U1-PadJ16) -> /DRAM_ADDR_13
- U1 pad J17: unconnected-(U1-PadJ17) -> /DRAM_ADDR_9
- U1 pad J3: unconnected-(U1-PadJ3) -> /VGA_B_4
- U1 pad J6: unconnected-(U1-PadJ6) -> Net-(U1-PadH6)
- U1 pad J8: unconnected-(U1-PadJ8) -> /FPGA_VCORE
- U1 pad K1: unconnected-(U1-PadK1) -> /VGA_G_3
- U1 pad K13: unconnected-(U1-PadK13) -> /FPGA_VCORE
- U1 pad K2: unconnected-(U1-PadK2) -> /VGA_B_2
- U1 pad K8: unconnected-(U1-PadK8) -> /FPGA_VCORE
- U1 pad L1: unconnected-(U1-PadL1) -> /VGA_R_3
- U1 pad L13: unconnected-(U1-PadL13) -> /FPGA_VCORE
- U1 pad L14: unconnected-(U1-PadL14) -> +1V35
- U1 pad L15: unconnected-(U1-PadL15) -> +1V35
- U1 pad L16: unconnected-(U1-PadL16) -> /DRAM_ADDR_8
- U1 pad L17: unconnected-(U1-PadL17) -> /DRAM_ADDR_14
- U1 pad L18: unconnected-(U1-PadL18) -> /DRAM_ADDR_6
- U1 pad L2: unconnected-(U1-PadL2) -> /VGA_R_2
- U1 pad L3: unconnected-(U1-PadL3) -> /VGA_G_2
- U1 pad L6: unconnected-(U1-PadL6) -> Net-(U1-PadL6)
- U1 pad L7: unconnected-(U1-PadL7) -> Net-(U1-PadL6)
- U1 pad L8: unconnected-(U1-PadL8) -> /FPGA_VCORE
- U1 pad M1: unconnected-(U1-PadM1) -> /VGA_B_1
- U1 pad M13: unconnected-(U1-PadM13) -> /FPGA_VCORE
- U1 pad M15: unconnected-(U1-PadM15) -> +1V35
- U1 pad M17: unconnected-(U1-PadM17) -> /DRAM_DQS1_N
- U1 pad M6: unconnected-(U1-PadM6) -> Net-(U1-PadL6)
- U1 pad M8: unconnected-(U1-PadM8) -> /FPGA_VCORE
- U1 pad N1: unconnected-(U1-PadN1) -> /VGA_G_1
- U1 pad N10: unconnected-(U1-PadN10) -> /FPGA_VCORE
- U1 pad N11: unconnected-(U1-PadN11) -> /FPGA_VCORE
- U1 pad N12: unconnected-(U1-PadN12) -> /FPGA_VCORE
- U1 pad N13: unconnected-(U1-PadN13) -> /FPGA_VCORE
- U1 pad N16: unconnected-(U1-PadN16) -> /DRAM_DQS1_P
- U1 pad N2: unconnected-(U1-PadN2) -> /VGA_G_0
- U1 pad N3: unconnected-(U1-PadN3) -> /VGA_B_0
- U1 pad N8: unconnected-(U1-PadN8) -> /FPGA_VCORE
- U1 pad N9: unconnected-(U1-PadN9) -> /FPGA_VCORE
- U1 pad P1: unconnected-(U1-PadP1) -> /VGA_R_1
- U1 pad P2: unconnected-(U1-PadP2) -> /VGA_R_0
- U1 pad P3: unconnected-(U1-PadP3) -> /VGA_VSYNC
- U1 pad P4: unconnected-(U1-PadP4) -> /VGA_HSYNC
- U1 pad R16: unconnected-(U1-PadR16) -> /DRAM_ADDR_4
- U1 pad R17: unconnected-(U1-PadR17) -> /DRAM_ADDR_11
- U1 pad R18: unconnected-(U1-PadR18) -> /DRAM_DQS0_N
- U1 pad T17: unconnected-(U1-PadT17) -> /DRAM_ADDR_BA1
- U1 pad T18: unconnected-(U1-PadT18) -> /DRAM_ADDR_1
- U1 pad T19: unconnected-(U1-PadT19) -> /DRAM_DQS0_P
- U1 pad U16: unconnected-(U1-PadU16) -> /DRAM_ADDR_10
- U1 pad U17: unconnected-(U1-PadU17) -> /DRAM_ADDR_15
- U1 pad U18: unconnected-(U1-PadU18) -> /DRAM_ADDR_12
- U1 pad Y11: unconnected-(U1-PadY11) -> /PCIE_REFCLK_P
- U1 pad Y12: unconnected-(U1-PadY12) -> /PCIE_REFCLK_N
- U10 pad 2: unconnected-(U10-Pad2) -> /VGA_R_4
- U10 pad 20: unconnected-(U10-Pad20) -> +3V3
- U10 pad 3: unconnected-(U10-Pad3) -> /VGA_R_5
- U10 pad 4: unconnected-(U10-Pad4) -> /VGA_G_4
- U10 pad 5: unconnected-(U10-Pad5) -> /VGA_G_5
- U10 pad 6: unconnected-(U10-Pad6) -> /VGA_B_4
- U10 pad 7: unconnected-(U10-Pad7) -> /VGA_B_5
- U5 pad 4: unconnected-(U5-Pad4) -> GND
- U5 pad 8: unconnected-(U5-Pad8) -> +3V3
- U6 pad 15: unconnected-(U6-Pad15) -> Net-(C56-Pad1)
- U6 pad 26: unconnected-(U6-Pad26) -> Net-(C56-Pad1)
- U6 pad 29: unconnected-(U6-Pad29) -> Net-(C57-Pad2)
- U6 pad 31: unconnected-(U6-Pad31) -> +3V3
- U6 pad 32: unconnected-(U6-Pad32) -> Net-(U6-Pad32)
- U6 pad 4: unconnected-(U6-Pad4) -> Net-(U6-Pad4)
- U7 pad 10: unconnected-(U7-Pad10) -> /SLAVE_EXTvBUS
- U7 pad 4: unconnected-(U7-Pad4) -> Net-(U7-Pad4)
- U8 pad 17: /VGA_VSYNC -> /VGA_BUF_VSYNC
- U8 pad 18: /VGA_HSYNC -> /VGA_BUF_HSYNC
- U8 pad 2: unconnected-(U8-Pad2) -> /VGA_HSYNC
- U8 pad 20: unconnected-(U8-Pad20) -> +3V3
- U8 pad 3: unconnected-(U8-Pad3) -> /VGA_VSYNC
- U8 pad 4: unconnected-(U8-Pad4) -> /VGA_R_0
- U8 pad 5: unconnected-(U8-Pad5) -> /VGA_R_1
- U8 pad 6: unconnected-(U8-Pad6) -> /VGA_G_0
- U8 pad 7: unconnected-(U8-Pad7) -> /VGA_G_1
- U8 pad 8: unconnected-(U8-Pad8) -> /VGA_B_0
- U8 pad 9: unconnected-(U8-Pad9) -> /VGA_B_1
- U9 pad 2: unconnected-(U9-Pad2) -> /VGA_R_2
- U9 pad 20: unconnected-(U9-Pad20) -> +3V3
- U9 pad 3: unconnected-(U9-Pad3) -> /VGA_R_3
- U9 pad 4: unconnected-(U9-Pad4) -> /VGA_G_2
- U9 pad 5: unconnected-(U9-Pad5) -> /VGA_G_3
- U9 pad 6: unconnected-(U9-Pad6) -> /VGA_B_2
- U9 pad 7: unconnected-(U9-Pad7) -> /VGA_B_3
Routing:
- net GND: track 23.6 -> 330.9 mm, vias 0 -> 58
- net +3V3: track 0.00 -> 68.7 mm, vias 0 -> 11
- net /DRAM_1_VCORE: track 0.00 -> 46.8 mm, vias 0 -> 15
- net /DRAM_2_VCORE: track 0.00 -> 41.6 mm, vias 0 -> 16
- net /DRAM_ADDR_10: track 0.00 -> 39.9 mm, vias 0 -> 4
- net /DRAM_nWE: track 0.00 -> 38.9 mm, vias 0 -> 4
- net /DRAM_ADDR_12: track 0.00 -> 37.8 mm, vias 0 -> 4
- net /DRAM_ADDR_15: track 0.00 -> 35.4 mm, vias 0 -> 4
- net /DRAM_ADDR_0: track 0.00 -> 35.3 mm, vias 0 -> 4
- net /DRAM_ADDR_BA0: track 0.00 -> 34.9 mm, vias 0 -> 4
- net /DRAM_ADDR_3: track 0.00 -> 34.1 mm, vias 0 -> 4
- net /DRAM_ADDR_BA2: track 0.00 -> 34.0 mm, vias 0 -> 4
- net /DRAM_ADDR_BA1: track 0.00 -> 32.6 mm, vias 0 -> 4
- net /DRAM_ADDR_1: track 0.00 -> 32.1 mm, vias 0 -> 4
- net /DRAM_nCS: track 0.00 -> 31.9 mm, vias 0 -> 4
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- added copper zone on In3.Cu, net +3V3
- added copper zone on In4.Cu, net /DRAM_1_VCORE
- added copper zone on In4.Cu, net /DRAM_2_VCORE
- added copper zone on In1.Cu, net GND
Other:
- board outline added: 100 x 90 mm

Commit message: ech
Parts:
- C40: moved to F.Cu
- moved C2 120.4 mm to (275.3, 118.9), turned to 0 degrees
- moved C3 117.1 mm to (272.4, 120.8), turned to 0 degrees
- moved C36 116.2 mm to (272.4, 122.8), turned to 0 degrees
- moved C37 103.7 mm to (258.3, 134.9), turned to 0 degrees
- moved C7 103.4 mm to (272.4, 118.9)
- moved C19 100.0 mm to (255.4, 136.9), turned to 0 degrees
- moved C5 99.0 mm to (255.4, 134.9), turned to 0 degrees
- moved C8 96.5 mm to (258.3, 136.9)
- moved C12 95.9 mm to (252.1, 140.4), turned to 0 degrees
- moved C35 95.0 mm to (249.2, 141.4), turned to 0 degrees
- moved C6 91.9 mm to (243.4, 142.9), turned to 0 degrees
- moved C18 90.4 mm to (246.3, 138.9), turned to 0 degrees
- moved C13 87.1 mm to (240.5, 140.9), turned to 0 degrees
- moved C20 86.2 mm to (246.2, 142.9), turned to 0 degrees
- moved C17 82.5 mm to (249.2, 139.4)
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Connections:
- RN6 pad 3: /DRAM_ADDR_14 -> /DRAM_ADDR_8
- RN6 pad 4: /DRAM_ADDR_8 -> /DRAM_ADDR_14
- RN7 pad 1: /DRAM_ADDR_15 -> /DRAM_ADDR_BA1
- RN7 pad 2: /DRAM_ADDR_BA1 -> /DRAM_ADDR_12
- RN8 pad 4: /DRAM_ADDR_12 -> /DRAM_ADDR_15
- U1 pad A12: unconnected-(U1-PadA12) -> Net-(U1-PadE11)
- U1 pad A13: unconnected-(U1-PadA13) -> Net-(U1-PadE11)
- U1 pad A14: unconnected-(U1-PadA14) -> Net-(U1-PadE11)
- U1 pad A16: unconnected-(U1-PadA16) -> Net-(U1-PadE11)
- U1 pad A17: unconnected-(U1-PadA17) -> Net-(U1-PadE11)
- U1 pad A18: unconnected-(U1-PadA18) -> Net-(U1-PadE11)
- U1 pad A19: unconnected-(U1-PadA19) -> Net-(U1-PadE11)
- U1 pad A2: /FIFO_D1/TX -> unconnected-(U1-PadA2)
- U1 pad A3: /FIFO_D3 -> unconnected-(U1-PadA3)
- U1 pad A4: /FIFO_D5 -> unconnected-(U1-PadA4)
- U1 pad A5: /FIFO_D7 -> unconnected-(U1-PadA5)
- U1 pad B1: /USB_SLAVE_DATA0 -> unconnected-(U1-PadB1)
- U1 pad B12: unconnected-(U1-PadB12) -> Net-(U1-PadE11)
- U1 pad B13: unconnected-(U1-PadB13) -> Net-(U1-PadE11)
- U1 pad B15: unconnected-(U1-PadB15) -> Net-(U1-PadE11)
- U1 pad B16: unconnected-(U1-PadB16) -> Net-(U1-PadE11)
- U1 pad B17: unconnected-(U1-PadB17) -> Net-(U1-PadE11)
- U1 pad B18: unconnected-(U1-PadB18) -> Net-(U1-PadE11)
- U1 pad B19: unconnected-(U1-PadB19) -> Net-(U1-PadE11)
- U1 pad B2: /USB_SLAVE_DATA1 -> unconnected-(U1-PadB2)
- U1 pad B20: unconnected-(U1-PadB20) -> Net-(U1-PadE11)
- U1 pad B3: /FIFO_D0/RX -> /DRAM_DATA_6
- U1 pad B4: /FIFO_D2 -> /DRAM_DATA_4
- U1 pad B5: /FIFO_D4 -> unconnected-(U1-PadB5)
- U1 pad C1: /USB_SLAVE_DATA2 -> unconnected-(U1-PadC1)
- U1 pad C12: unconnected-(U1-PadC12) -> Net-(U1-PadE11)
- U1 pad C13: unconnected-(U1-PadC13) -> Net-(U1-PadE11)
- U1 pad C14: unconnected-(U1-PadC14) -> Net-(U1-PadE11)
- U1 pad C15: unconnected-(U1-PadC15) -> Net-(U1-PadE11)
- U1 pad C16: unconnected-(U1-PadC16) -> Net-(U1-PadE11)
- U1 pad C17: unconnected-(U1-PadC17) -> Net-(U1-PadE11)
- U1 pad C18: /DRAM_nWE -> /DRAM_DM2
- U1 pad C2: /USB_SLAVE_DATA3 -> unconnected-(U1-PadC2)
- U1 pad C20: /DRAM_nCS -> unconnected-(U1-PadC20)
- U1 pad C3: /FIFO_nTXE -> unconnected-(U1-PadC3)
- U1 pad C4: /FIFO_nRXE -> /DRAM_DATA_5
- U1 pad C5: /FIFO_D6 -> /DRAM_DATA_7
- U1 pad D1: /USB_SLAVE_DATA4 -> unconnected-(U1-PadD1)
- U1 pad D11: unconnected-(U1-PadD11) -> Net-(U1-PadE11)
- U1 pad D12: unconnected-(U1-PadD12) -> Net-(U1-PadE11)
- U1 pad D13: unconnected-(U1-PadD13) -> Net-(U1-PadE11)
- U1 pad D14: unconnected-(U1-PadD14) -> Net-(U1-PadE11)
- U1 pad D15: unconnected-(U1-PadD15) -> Net-(U1-PadE11)
- U1 pad D16: unconnected-(U1-PadD16) -> Net-(U1-PadE11)
- U1 pad D17: /DRAM_ADDR_BA0 -> /DRAM_DATA_19
- U1 pad D18: /DRAM_ADDR_BA2 -> /DRAM_DATA_17
- U1 pad D19: unconnected-(U1-PadD19) -> /DRAM_DATA_30
- U1 pad D2: /USB_SLAVE_DATA5 -> unconnected-(U1-PadD2)
- U1 pad D3: /FIFO_nWR -> unconnected-(U1-PadD3)
- U1 pad D5: /FIFO_nRD -> /DRAM_DQS0_N
- U1 pad E1: /USB_SLAVE_DATA6 -> /DRAM_DATA_11
- U1 pad E11: unconnected-(U1-PadE11) -> Net-(U1-PadE11)
- U1 pad E12: unconnected-(U1-PadE12) -> Net-(U1-PadE11)
- U1 pad E13: unconnected-(U1-PadE13) -> Net-(U1-PadE11)
- U1 pad E14: unconnected-(U1-PadE14) -> Net-(U1-PadE11)
- U1 pad E15: unconnected-(U1-PadE15) -> Net-(U1-PadE11)
- U1 pad E16: /DRAM_ADDR_3 -> /DRAM_DATA_21
- U1 pad E17: /DRAM_ADDR_0 -> /DRAM_DATA_22
- U1 pad E18: unconnected-(U1-PadE18) -> /DRAM_DATA_23
- U1 pad E19: unconnected-(U1-PadE19) -> /DRAM_DATA_28
- U1 pad E2: /USB_SLAVE_DATA7 -> /DRAM_DATA_13
- U1 pad E3: /USB_SLAVE_RESET -> unconnected-(U1-PadE3)
- U1 pad E4: /USB_SLAVE_CLK -> /DRAM_DQS0_P
- U1 pad E5: /FIFO_WKUP -> unconnected-(U1-PadE5)
- U1 pad F16: unconnected-(U1-PadF16) -> /DRAM_DATA_18
- U1 pad F17: unconnected-(U1-PadF17) -> /DRAM_DQS2_P
- U1 pad F18: unconnected-(U1-PadF18) -> /DRAM_DATA_16
- U1 pad F19: unconnected-(U1-PadF19) -> /DRAM_DATA_26
- U1 pad F2: unconnected-(U1-PadF2) -> /DRAM_DATA_15
- U1 pad F3: /USB_SLAVE_NXT -> /DRAM_DATA_14
- U1 pad F4: /USB_SLAVE_DIR -> unconnected-(U1-PadF4)
- U1 pad F5: /USB_SLAVE_CLKOUT -> unconnected-(U1-PadF5)
- U1 pad G16: unconnected-(U1-PadG16) -> /DRAM_DATA_20
- U1 pad G18: unconnected-(U1-PadG18) -> /DRAM_DQS2_N
- U1 pad G19: unconnected-(U1-PadG19) -> /DRAM_DQS3_P
- U1 pad G20: unconnected-(U1-PadG20) -> /DRAM_DATA_24
- U1 pad G3: /USB_SLAVE_STP -> /DRAM_DATA_12
- U1 pad G5: unconnected-(U1-PadG5) -> /DRAM_DQS1_N
- U1 pad H20: unconnected-(U1-PadH20) -> /DRAM_DQS3_N
- U1 pad H3: unconnected-(U1-PadH3) -> /DRAM_DATA_8
- U1 pad H4: unconnected-(U1-PadH4) -> /DRAM_DQS1_P
- U1 pad H5: unconnected-(U1-PadH5) -> /DRAM_DATA_10
- U1 pad H6: Net-(U1-PadH6) -> unconnected-(U1-PadH6)
- U1 pad H7: Net-(U1-PadH6) -> unconnected-(U1-PadH7)
- U1 pad J16: /DRAM_ADDR_13 -> unconnected-(U1-PadJ16)
- U1 pad J17: /DRAM_ADDR_9 -> unconnected-(U1-PadJ17)
- U1 pad J18: unconnected-(U1-PadJ18) -> /DRAM_DM3
- U1 pad J19: unconnected-(U1-PadJ19) -> /DRAM_DATA_31
- U1 pad J20: unconnected-(U1-PadJ20) -> /DRAM_DATA_25
- U1 pad J6: Net-(U1-PadH6) -> unconnected-(U1-PadJ6)
- U1 pad K19: unconnected-(U1-PadK19) -> /DRAM_DATA_29
- U1 pad K20: unconnected-(U1-PadK20) -> /DRAM_DATA_27
- U1 pad L14: +1V35 -> unconnected-(U1-PadL14)
- U1 pad L15: +1V35 -> unconnected-(U1-PadL15)
- U1 pad L16: /DRAM_ADDR_8 -> unconnected-(U1-PadL16)
- U1 pad L17: /DRAM_ADDR_14 -> unconnected-(U1-PadL17)
- U1 pad L18: /DRAM_ADDR_6 -> unconnected-(U1-PadL18)
- U1 pad M15: +1V35 -> unconnected-(U1-PadM15)
- U1 pad M17: /DRAM_DQS1_N -> unconnected-(U1-PadM17)
- U1 pad N16: /DRAM_DQS1_P -> unconnected-(U1-PadN16)
- U1 pad R16: /DRAM_ADDR_4 -> unconnected-(U1-PadR16)
- U1 pad R17: /DRAM_ADDR_11 -> unconnected-(U1-PadR17)
- U1 pad R18: /DRAM_DQS0_N -> unconnected-(U1-PadR18)
- U1 pad T17: /DRAM_ADDR_BA1 -> unconnected-(U1-PadT17)
- U1 pad T18: /DRAM_ADDR_1 -> unconnected-(U1-PadT18)
- U1 pad T19: /DRAM_DQS0_P -> unconnected-(U1-PadT19)
- U1 pad U16: /DRAM_ADDR_10 -> unconnected-(U1-PadU16)
- U1 pad U17: /DRAM_ADDR_15 -> unconnected-(U1-PadU17)
- U1 pad U18: /DRAM_ADDR_12 -> unconnected-(U1-PadU18)
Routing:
- net GND: track 330.9 -> 135.2 mm, vias 58 -> 41
- net /DRAM_ADDR_10: track 39.9 -> 0.00 mm, vias 4 -> 0
- net /DRAM_nWE: track 38.9 -> 0.00 mm, vias 4 -> 0
- net /DRAM_1_VCORE: track 46.8 -> 7.98 mm, vias 15 -> 10
- net /DRAM_ADDR_12: track 37.8 -> 0.00 mm, vias 4 -> 0
- net /DRAM_ADDR_15: track 35.4 -> 0.00 mm, vias 4 -> 0
- net /DRAM_ADDR_0: track 35.3 -> 0.00 mm, vias 4 -> 0
- net /DRAM_ADDR_BA0: track 34.9 -> 0.00 mm, vias 4 -> 0
- net /DRAM_ADDR_3: track 34.1 -> 0.00 mm, vias 4 -> 0
- net /DRAM_ADDR_BA2: track 34.0 -> 0.00 mm, vias 4 -> 0
- net /DRAM_ADDR_BA1: track 32.6 -> 0.00 mm, vias 4 -> 0
- net /DRAM_nCS: track 31.9 -> 0.00 mm, vias 4 -> 0
- net /DRAM_2_VCORE: track 41.6 -> 10.1 mm, vias 16 -> 8
- net /DRAM_ADDR_1: track 32.1 -> 0.59 mm, vias 4 -> 1
- net /DRAM_ADDR_6: track 31.3 -> 0.56 mm, vias 4 -> 1
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- removed copper zone on In4.Cu, net /DRAM_1_VCORE
- removed copper zone on In4.Cu, net /DRAM_2_VCORE
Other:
- board text added: "DRAM STACKUP F1.cu V+ In1.Cu -signal In2.Cu - ground In3.Cu - signal In4.Cu - signal B.Cu - ground"
